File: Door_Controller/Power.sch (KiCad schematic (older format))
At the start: 10 parts

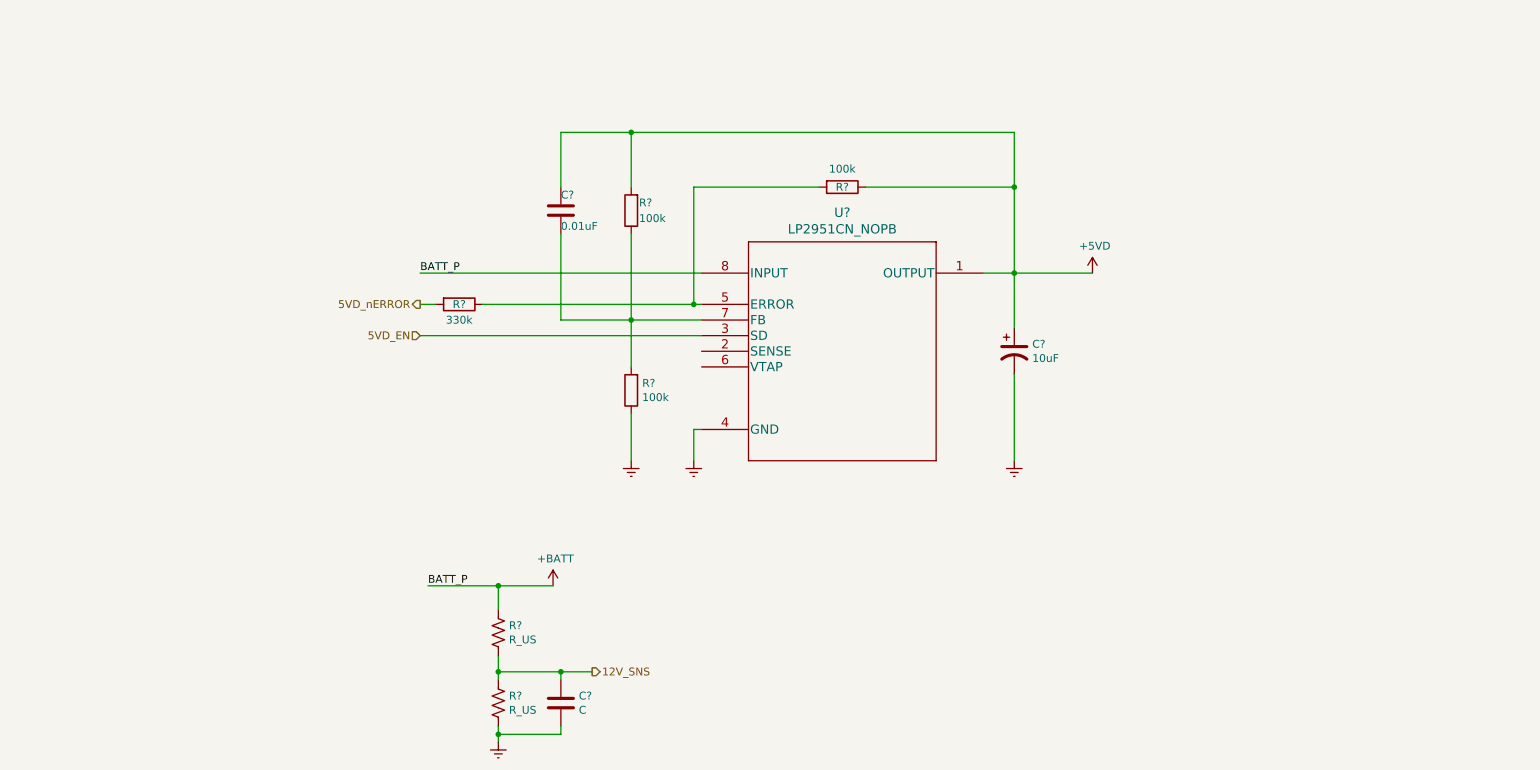
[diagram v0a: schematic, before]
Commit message: add V3p3 power rail
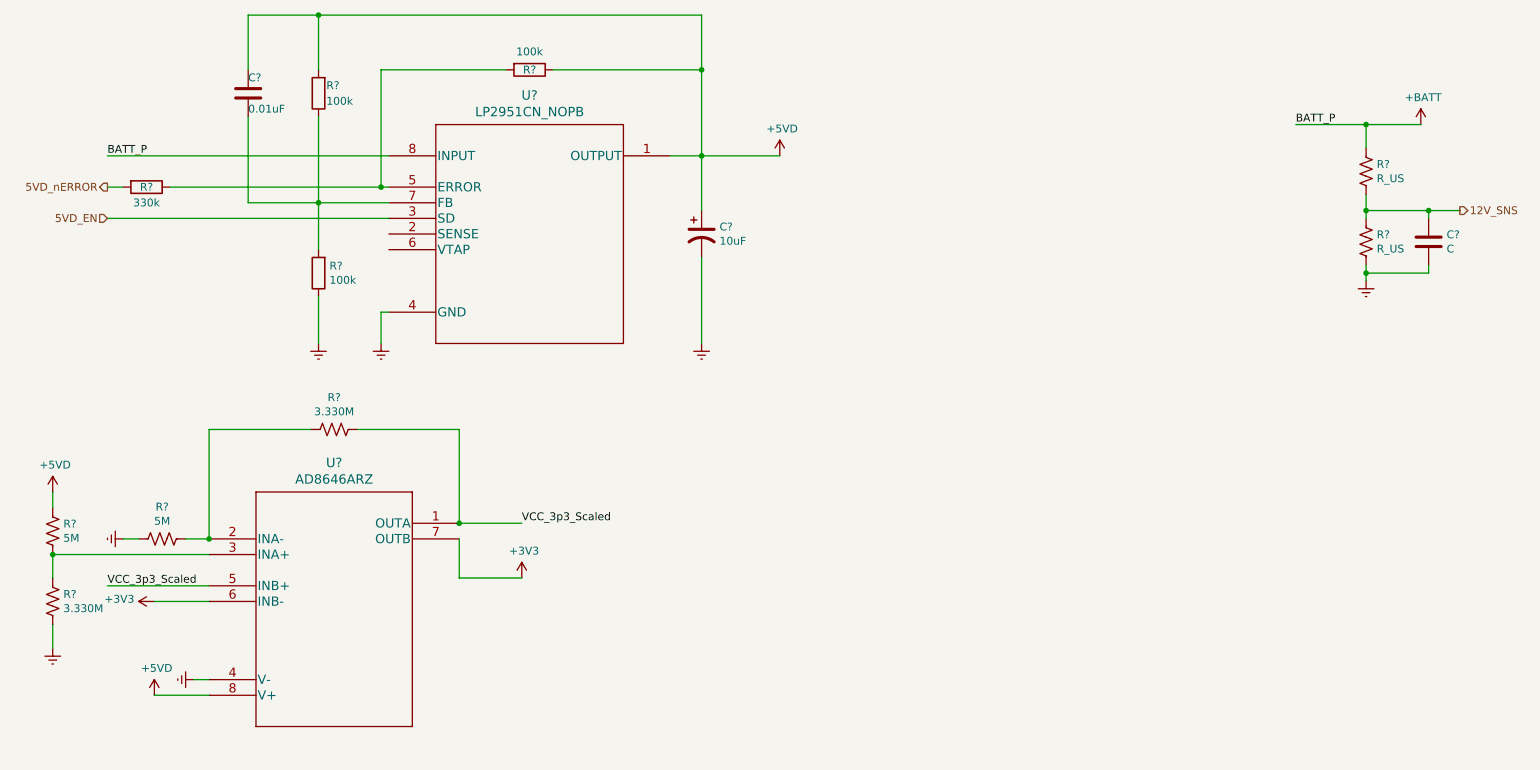
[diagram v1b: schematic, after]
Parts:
- added R? (x2): 5M, symbol Device:R_US
- added R? (x2): 3.330M, symbol Device:R_US
- added U?: AD8646ARZ, R_8_ADI, symbol AD8646ARZ:AD8646ARZ
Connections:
- net +5VD: now also R?.1, U?.8 (V+)
- net Earth: now also R?.2, R?.2, U?.4 (V-)
- new net: R?.1, R?.2, U?.2 (INA-)
- new net: R?.1, R?.2, U?.3 (INA+)
- new net +3V3: U?.6 (INB-), U?.7 (OUTB)
- new net VCC_3p3_Scaled: R?.1, U?.1 (OUTA), U?.5 (INB+)
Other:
- moved on the sheet: C?, R?, U?
